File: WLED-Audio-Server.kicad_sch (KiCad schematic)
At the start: 25 parts, among them J1 AudioJack4, J2 AudioJack4, SW1 SW_Push, U1 LMV358, U2 ESP32-DEVKIT-V1

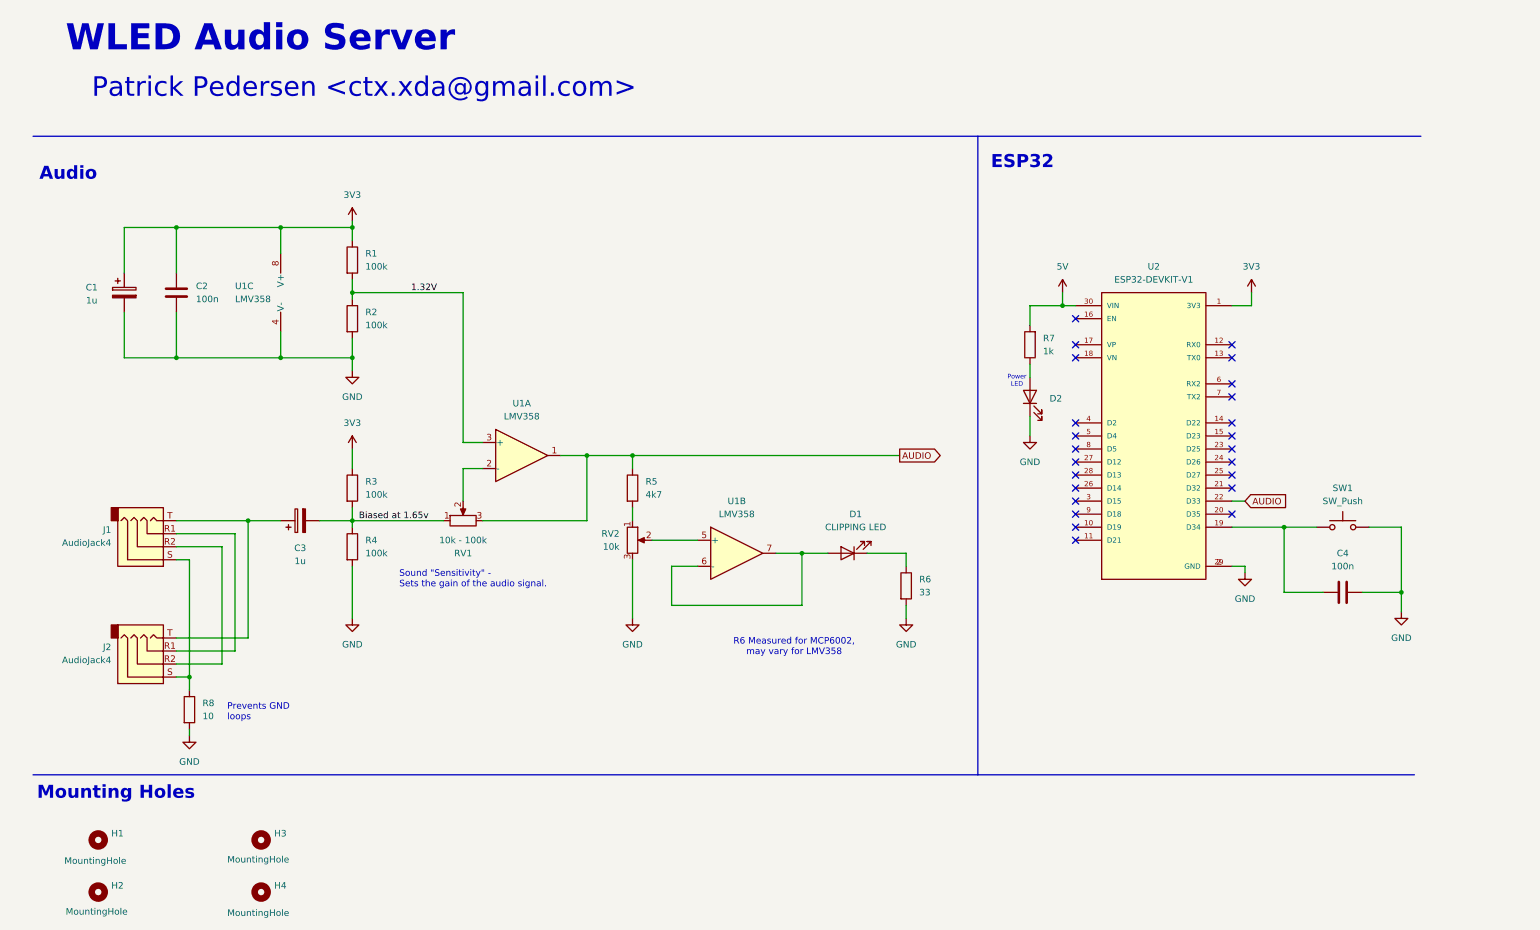
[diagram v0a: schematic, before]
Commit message: Revision 1.0.1: Fixed potentiometer orientation + PB Pitch
Signed-off-by: Patrick Pedersen <ctx.xda@gmail.com>
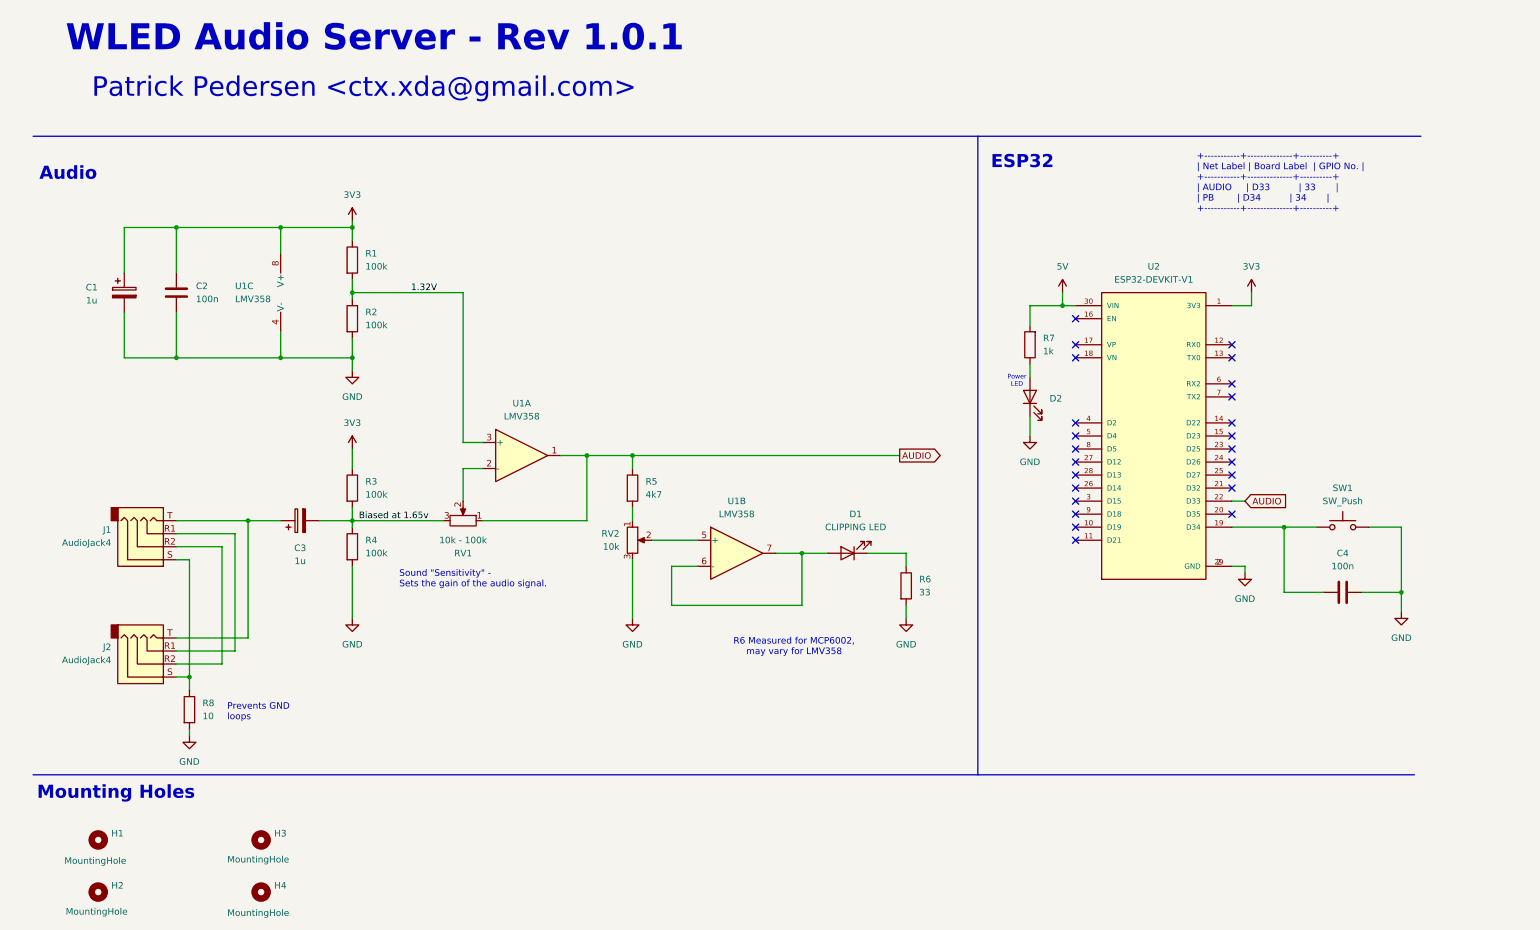
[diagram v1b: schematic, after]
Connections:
- net AUDIO: now also RV1.1; no longer RV1.3
- net Biased at 1.65v: now also RV1.3; no longer RV1.1
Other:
- note added: "+-----------+--------------+----------+ | Net Label | Board Label | GPIO No. | +-----------+--------------+----------+ | AUDIO | D33 | 33 | | PB | D34 | 34 | +-----------+--------------+----------+"
- note added: "WLED Audio Server - Rev 1.0.1"
- note removed: "WLED Audio Server"
- moved on the sheet: RV1
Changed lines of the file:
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@@
 		)
 	)
-	(text "WLED Audio Server"
+	(text "+-----------+--------------+----------+\n| Net Label | Board Label  | GPIO No. |\n+-----------+--------------+----------+\n| AUDIO     | D33          | 33       |\n| PB        | D34          | 34       |\n+-----------+--------------+----------+"
+		(exclude_from_sim no)
+		(at 239.522 49.784 0)
+		(effects
+			(font
+				(face "DejaVu Sans Mono")
+				(size 1.27 1.27)
+			)
+			(justify left)
+		)
+	)
+	(text "WLED Audio Server - Rev 1.0.1"
 		(exclude_from_sim no)
 		(at 19.05 21.59 0)
@@
 	(symbol
 		(lib_id "Device:R_Potentiometer")
-		(at 96.52 115.57 90)
+		(at 96.52 115.57 270)
+		(mirror x)
 		(unit 1)
 		(exclude_from_sim no)
